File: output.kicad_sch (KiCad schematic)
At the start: 29 parts

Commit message: Schematic is basically feature complete
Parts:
- added C112, C122, C131: 0u1, Capacitor_SMD:C_0402_1005Metric, symbol Device:C
- added D13, D14, D21, D22, D3, D4: D_TVS, Diode_SMD:D_0402_1005Metric_Pad0.77x0.64mm_HandSolder, symbol Device:D_TVS
- C13, C14, C21, C22: renamed from C?; value 1n -> 10n
- J1, J2, J3, J4: renamed from J?; value Conn_Coaxial -> SMA; now left out of the parts list
- R112, R122: renamed from R?; value 2k7 -> 3k3
- R113, R123: renamed from R?; value 1k -> 100k
- T1, T2: renamed from T?; MANUFACTURER M/A-Com Technology Solutions -> (none); PARTREV v5 -> (none); STANDARD Manufacturer Recommendations -> (none)
- U11, U12: renamed from U?; footprint (none) -> Package_TO_SOT_SMD:SOT-353_SC-70-5; now left out of the parts list
- U13: renamed from U?; value TS5A23159DGS -> TS5A23157DGS; now left out of the parts list
- gave numbers to parts that had none: 10
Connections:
- net EN_OUT4: now also U11.1
- net GND: now also U13.3 (GND), C112.2, C122.2, C131.2, D13.1 (A1), D14.2 (A2), D21.1 (A1), D22.2 (A2), D3.1 (A1), D4.1 (A1)
- net OUT0_N: now also D14.1 (A1)
- net OUT0_P: now also D13.2 (A2)
- net OUT2_N: now also D22.1 (A1)
- net OUT2_P: now also D21.2 (A2)
- net OUT7_P: no longer R121.1, R124.1
- net at J4.1 (In), U13.4: now also U13.9, D4.2 (A2); no longer U13.2
- net at C121.1, D12.1 (K), R121.2: now also R122.2
- net at C121.2, D12.2 (A), R123.1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: no longer R122.2
- net EN_OUT3: now reaches U12.1
- net +3V3: now reaches R123.2, U12.5 (VCC)
- net +3V3: now also R113.2, U11.5 (VCC), U13.8 (VCC), C112.1, C122.1, C131.1
- net at J3.1 (In), R124.2, R125.2: now also D3.2 (A2)
- net at C111.1, D11.1 (K), R111.2: now also R112.2
- net at C111.2, D11.2 (A), R113.1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: no longer R112.2
- new net OUT7_N: R121.1, R124.1
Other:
- note added: "TODO - check component values"
- note added: "TODO - check polarity & pull"
- note added: "TODO - which rail for these?"
- moved on the sheet: C111, C121, C13, C14, C21, C22, D11, D12, J1, J2, J3, J4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

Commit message: Sorting out the part placement....
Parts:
- R112, R113, R122, R123: footprint Resistor_SMD:R_0603_1608Metric -> Resistor_SMD:R_0402_1005Metric
- T1, T2: footprint MABA-007159-000000:XFMR_MABA-007159-000000 -> Parts:XFMR_MABA-007159-000000
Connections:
- net EN_OUT3: now also U11.1; no longer U12.1
- net EN_OUT4: now also U12.1; no longer U11.1
- net OUT7_N: now also R111.1, R114.1; no longer R121.1, R124.1
- net OUT7_P: now also R121.1, R124.1; no longer R111.1, R114.1
- net Conn4: now reaches D4.2 (A2), J4.1 (In), U13.4, U13.9
- net at R115.1: now also U12.4; no longer U11.4
- net Ext4: now reaches R114.2, R115.2, U13.10
- net at C121.2, D12.2 (A), R123.1: now also U11.2; no longer U12.2
- net Ext3: now reaches D3.2 (A2), J3.1 (In), R124.2, R125.2
- net AC0_P: now reaches C13.2, T1.1
- net at R125.1: now also U11.4; no longer U12.4
- net AC2_N: now reaches C22.2, T2.3
- net AC2_P: now reaches C21.2, T2.1
- net Ext2: now reaches J2.1 (In), T2.5
- net at C111.2, D11.2 (A), R113.1: now also U12.2; no longer U11.2
- net AC0_N: now reaches C14.2, T1.3
- net Ext1: now reaches J1.1 (In), T1.5
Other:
- note removed: "TODO - protection"
- moved on the sheet: U11, U12
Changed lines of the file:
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@@
 		)
 	)
-	(text "TODO - protection"
-		(exclude_from_sim no)
-		(at 184.658 79.248 0)
-		(effects
-			(font
-				(size 1.27 1.27)
-			)
-			(justify left top)
-		)
-	)
 	(text "TODO - which rail for these?"
 		(exclude_from_sim no)
@@
 		)
 	)
+	(label "AC2_P"
+		(at 187.96 52.07 0)
+		(effects
+			(font
+				(size 1.27 1.27)
+			)
+			(justify left bottom)
+		)
+	)
+	(label "Ext3"
+		(at 167.64 138.43 90)
+		(effects
+			(font
+				(size 1.27 1.27)
+			)
+			(justify left bottom)
+		)
+	)
+	(label "Ext4"
+		(at 167.64 101.6 90)
+		(effects
+			(font
+				(size 1.27 1.27)
+			)
+			(justify left bottom)
+		)
+	)
+	(label "AC0_N"
+		(at 99.06 62.23 0)
+		(effects
+			(font
+				(size 1.27 1.27)
+			)
+			(justify left bottom)
+		)
+	)
+	(label "Ext1"
+		(at 127 52.07 0)
+		(effects
+			(font
+				(size 1.27 1.27)
+			)
+			(justify left bottom)
+		)
+	)
+	(label "AC0_P"
+		(at 99.06 52.07 0)
+		(effects
+			(font
+				(size 1.27 1.27)
+			)
+			(justify left bottom)
+		)
+	)
+	(label "Ext2"
+		(at 215.9 52.07 0)
+		(effects
+			(font
+				(size 1.27 1.27)
+			)
+			(justify left bottom)
+		)
+	)
+	(label "Conn4"
+		(at 205.74 104.14 90)
+		(effects
+			(font
+				(size 1.27 1.27)
+			)
+			(justify left bottom)
+		)
+	)
+	(label "AC2_N"
+		(at 187.96 62.23 0)
+		(effects
+			(font
+				(size 1.27 1.27)
+			)
+			(justify left bottom)
+		)
+	)
 	(global_label "EN_REF2"
 		(shape input)
@@
 	(global_label "OUT7_N"
 		(shape input)
-		(at 102.87 127 180)
+		(at 102.87 90.17 180)
 		(fields_autoplaced yes)
 		(effects
@@
 		)
 		(property "Intersheetrefs" "${INTERSHEET_REFS}"
-			(at 92.7486 127 0)
+			(at 92.8091 90.17 0)
 			(effects
 				(font
@@
 	(global_label "OUT7_P"
 		(shape input)
-		(at 102.87 90.17 180)
+		(at 102.87 127 180)
 		(fields_autoplaced yes)
 		(effects
@@
 		)
 		(property "Intersheetrefs" "${INTERSHEET_REFS}"
-			(at 92.8091 90.17 0)
+			(at 92.7486 127 0)
 			(effects
 				(font
@@
 		(length 2.54)
 		(shape round)
-		(at 190.5 62.23 0)
+		(at 190.5 52.07 180)
 		(effects
 			(font
 				(size 1.27 1.27)
 			)
-			(justify left bottom)
+			(justify right bottom)
 		)
 		(property "Netclass" "50diff"
-			(at 190.5 58.928 0)
+			(at 190.5 55.372 0)
 			(effects
 				(font
 					(size 1.27 1.27)
 				)
-				(justify bottom)
+				(justify top)
 			)
 		)
 		(property "Component Class" ""
-			(at 161.29 43.18 0)
+			(at 161.29 71.12 0)
 			(effects
 				(font
@@
 		(length 2.54)
 		(shape round)
-		(at 190.5 52.07 0)
+		(at 190.5 62.23 180)
 		(effects
 			(font
 				(size 1.27 1.27)
 			)
-			(justify left bottom)
+			(justify right bottom)
 		)
 		(property "Netclass" "50diff"
-			(at 190.5 48.768 0)
+			(at 190.5 65.532 0)
 			(effects
 				(font
 					(size 1.27 1.27)
 				)
-				(justify bottom)
+				(justify top)
 			)
 		)
 		(property "Component Class" ""
-			(at 161.29 33.02 0)
+			(at 161.29 81.28 0)
 			(effects
 				(font
@@
 		(length 2.54)
 		(shape round)
-		(at 217.17 52.07 0)
+		(at 213.36 52.07 0)
 		(effects
 			(font
@@
 		)
 		(property "Netclass" "50cop"
-			(at 217.17 48.768 0)
+			(at 213.36 48.768 0)
 			(effects
 				(font
@@
 		)
 		(property "Component Class" ""
-			(at 187.96 33.02 0)
+			(at 184.15 33.02 0)
 			(effects
 				(font
@@
 		(length 2.54)
 		(shape round)
-		(at 128.27 52.07 0)
+		(at 124.46 52.07 0)
 		(effects
 			(font
@@
 		)
 		(property "Netclass" "50cop"
-			(at 128.27 48.768 0)
+			(at 124.46 48.768 0)
 			(effects
 				(font
@@
 		)
 		(property "Component Class" ""
-			(at 99.06 33.02 0)
+			(at 95.25 33.02 0)
 			(effects
 				(font
@@
 		(length 2.54)
 		(shape round)
-		(at 101.6 52.07 0)
+		(at 101.6 52.07 180)
 		(effects
 			(font
 				(size 1.27 1.27)
 			)
-			(justify left bottom)
+			(justify right bottom)
 		)
 		(property "Netclass" "50diff"
-			(at 101.6 48.768 0)
+			(at 101.6 55.372 0)
 			(effects
 				(font
 					(size 1.27 1.27)
 				)
-				(justify bottom)
+				(justify top)
 			)
 		)
 		(property "Component Class" ""
-			(at 72.39 33.02 0)
+			(at 72.39 71.12 0)
 			(effects
 				(font
@@
 		(length 2.54)
 		(shape round)
-		(at 101.6 62.23 0)
+		(at 101.6 62.23 180)
 		(effects
 			(font
 				(size 1.27 1.27)
 			)
-			(justify left bottom)
+			(justify right bottom)
 		)
 		(property "Netclass" "50diff"
-			(at 101.6 58.928 0)
+			(at 101.6 65.532 0)
 			(effects
 				(font
 					(size 1.27 1.27)
 				)
-				(justify bottom)
+				(justify top)
 			)
 		)
 		(property "Component Class" ""
-			(at 72.39 43.18 0)
+			(at 72.39 81.28 0)
 			(effects
 				(font
@@
 	(symbol
 		(lib_id "74xGxx:74LVC1G125")
-		(at 146.05 127 0)
+		(at 146.05 90.17 0)
 		(unit 1)
 		(exclude_from_sim no)
@@
 		(dnp no)
 		(property "Reference" "U12"
-			(at 145.542 126.746 0)
+			(at 145.542 89.916 0)
 			(effects
 				(font
@@
 		)
 		(property "Value" "74LVC1G125"
-			(at 147.828 133.35 0)
+			(at 147.828 96.52 0)
 			(effects
 				(font
@@
 		)
 		(property "Footprint" "Package_TO_SOT_SMD:SOT-353_SC-70-5"
-			(at 146.05 127 0)
+			(at 146.05 90.17 0)
 			(effects
 				(font
@@
 		)
 		(property "Datasheet" "https://www.ti.com/lit/ds/symlink/sn74lvc1g125.pdf"
-			(at 146.05 127 0)
+			(at 146.05 90.17 0)
 			(effects
 				(font
@@
 		)
 		(property "Description" "Single Buffer Gate Tri-State, Low-Voltage CMOS"
-			(at 146.05 127 0)
+			(at 146.05 90.17 0)
 			(effects
 				(font
@@
 			)
 		)
-		(property "Footprint" "MABA-007159-000000:XFMR_MABA-007159-000000"
+		(property "Footprint" "Parts:XFMR_MABA-007159-000000"
 			(at 203.2 57.15 0)
 			(effects
@@
 		(pin "5"
 		)
+		(pin "2"
+		)
 		(instances
 			(project "gpsref"
@@
 			)
 		)
-		(property "Footprint" "Resistor_SMD:R_0603_1608Metric"
+		(property "Footprint" "Resistor_SMD:R_0402_1005Metric"
 			(at 132.588 83.82 90)
 			(effects
@@
 			)
 		)
-		(property "Footprint" "Resistor_SMD:R_0603_1608Metric"
+		(property "Footprint" "Resistor_SMD:R_0402_1005Metric"
 			(at 120.65 135.382 90)
 			(effects
@@
 			)
 		)
-		(property "Footprint" "MABA-007159-000000:XFMR_MABA-007159-000000"
+		(property "Footprint" "Parts:XFMR_MABA-007159-000000"
 			(at 114.3 57.15 0)
 			(effects
@@
 		(pin "5"
 		)
+		(pin "2"
+		)
 		(instances
 			(project ""
@@
 			)
 		)
-		(property "Footprint" "Resistor_SMD:R_0603_1608Metric"
+		(property "Footprint" "Resistor_SMD:R_0402_1005Metric"
 			(at 120.65 98.552 90)
 			(effects
@@
 	(symbol
 		(lib_id "74xGxx:74LVC1G125")
-		(at 146.05 90.17 0)
+		(at 146.05 127 0)
 		(unit 1)
 		(exclude_from_sim no)
@@
 		(dnp no)
 		(property "Reference" "U11"
-			(at 146.05 90.17 0)
+			(at 146.05 127 0)
 			(effects
 				(font
@@
 		)
 		(property "Value" "74LVC1G125"
-			(at 147.828 96.52 0)
+			(at 147.828 133.35 0)
 			(effects
 				(font
@@
 		)
 		(property "Footprint" "Package_TO_SOT_SMD:SOT-353_SC-70-5"
-			(at 146.05 90.17 0)
+			(at 146.05 127 0)
 			(effects
 				(font
@@
 		)
 		(property "Datasheet" "https://www.ti.com/lit/ds/symlink/sn74lvc1g125.pdf"
-			(at 146.05 90.17 0)
+			(at 146.05 127 0)
 			(effects
 				(font
@@
 		)
 		(property "Description" "Single Buffer Gate Tri-State, Low-Voltage CMOS"
-			(at 146.05 90.17 0)
+			(at 146.05 127 0)
 			(effects
 				(font
@@
 			)
 		)
-		(property "Footprint" "Resistor_SMD:R_0603_1608Metric"
+		(property "Footprint" "Resistor_SMD:R_0402_1005Metric"
 			(at 132.588 120.65 90)
 			(effects

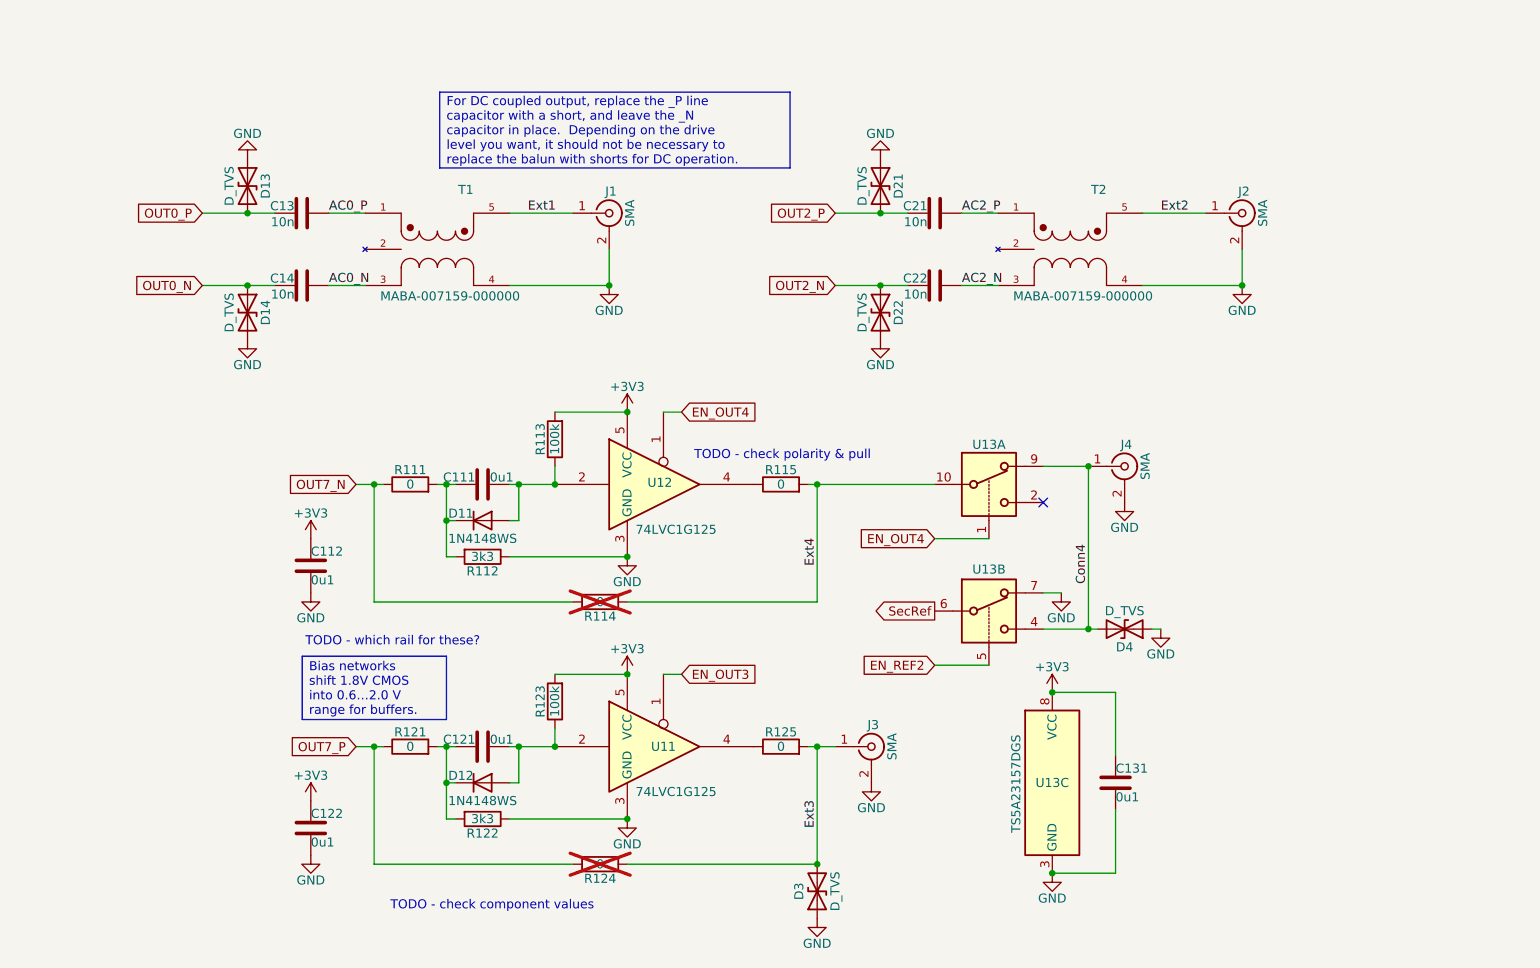
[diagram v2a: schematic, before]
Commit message: First round of component distribution
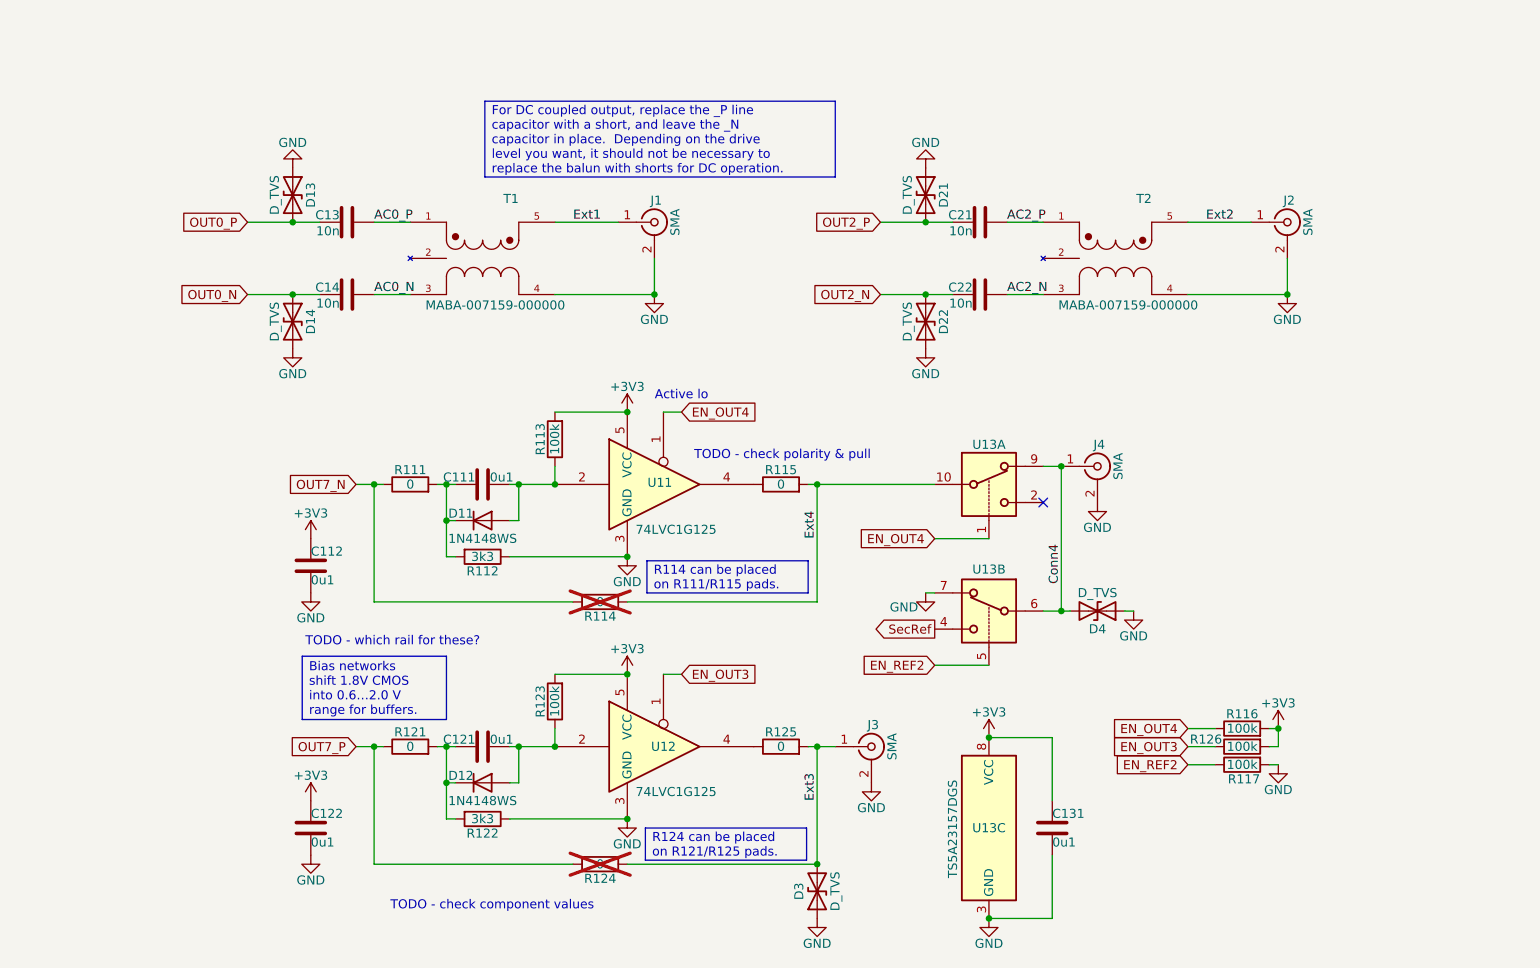
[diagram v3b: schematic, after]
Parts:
- added R116, R117, R126: 100k, Resistor_SMD:R_0402_1005Metric, symbol Device:R
- R114, R124: now left out of the parts list
- renumbered U12 to U11, U11 to U12
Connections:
- net +3V3: now also R116.2, R126.2
- net Conn4: now also U13.6; no longer U13.4
- net EN_OUT3: now also R126.1
- net EN_OUT4: now also R116.1
- net EN_REF2: now also R117.1
- net GND: now also R117.2
- net SecRef: now also U13.4; no longer U13.6
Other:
- note added: "Active lo"
- moved on the sheet: C13, C131, C14, C21, C22, D13, D14, D21, D22, D4, J1, J2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

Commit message: Placement looks sane.
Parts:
- removed U13: TS5A23157DGS, Package_SO:VSSOP-10_3x3mm_P0.5mm, symbol Analog_Switch:TS5A23159DGS
- added U13: TS5A63157DBV, Package_TO_SOT_SMD:SOT-23-6, symbol Analog_Switch:TS5A63157DBV
- U11, U12: footprint Package_TO_SOT_SMD:SOT-353_SC-70-5 -> Package_TO_SOT_SMD:SOT-23-5
- renumbered J2 to J1, J1 to J2
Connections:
- net +3V3: now also U13.5 (V+)
- net Conn4: now also U13.4
- net EN_REF2: now also U13.6
- net Ext4: now also U13.3
- net GND: now also U13.2 (GND)
- net SecRef: now also U13.1
- no-connect marks 1 -> 0
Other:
- moved on the sheet: D4, J4

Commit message: Routing well underway
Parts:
- added R118: 0, Resistor_SMD:R_0603_1608Metric, symbol Device:R
- D13, D14, D21, D22, D3: footprint Diode_SMD:D_0402_1005Metric_Pad0.77x0.64mm_HandSolder -> Parts:HHS_0402; symbol Device:D_TVS -> Parts:D_TVS; now in the parts list
- D4: value D_TVS -> BAS40-04; footprint Diode_SMD:D_0402_1005Metric_Pad0.77x0.64mm_HandSolder -> Package_TO_SOT_SMD:SOT-23; symbol Device:D_TVS -> Diode:BAS40-04; JLCPCB (none) -> C7502688; now in the parts list
- U11: value 74LVC1G125 -> 74LVC1G240; symbol 74xGxx:74LVC1G125 -> 74xGxx:74LVC1G240
- U13: now left out of the parts list
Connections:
- net +3V3: now also D4.2
- net Conn4: now also R118.2; no longer D4.2 (A2), U13.4
- net Ext3: now also D3.1 (A1); no longer D3.2 (A2)
- net GND: now also D13.2 (A2), D21.2 (A2), D3.2 (A2); no longer D13.1 (A1), D21.1 (A1), D3.1 (A1)
- net OUT0_P: now also D13.1 (A1); no longer D13.2 (A2)
- net OUT2_P: now also D21.1 (A1); no longer D21.2 (A2)
- new net: D4.3, R118.1, U13.4
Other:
- note removed: "TODO - check polarity & pull"
- moved on the sheet: J4, U13A
